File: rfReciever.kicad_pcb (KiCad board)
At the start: 2 copper layers, 5 x 8.2 mm, 37 parts, among them P2 USB_C_Plug_USB2.0, SW1 RF_RESET, SW2 RF_RESET, U1 CP2102N-Axx-xQFN20, X1 DigiXBeeRX900Micro

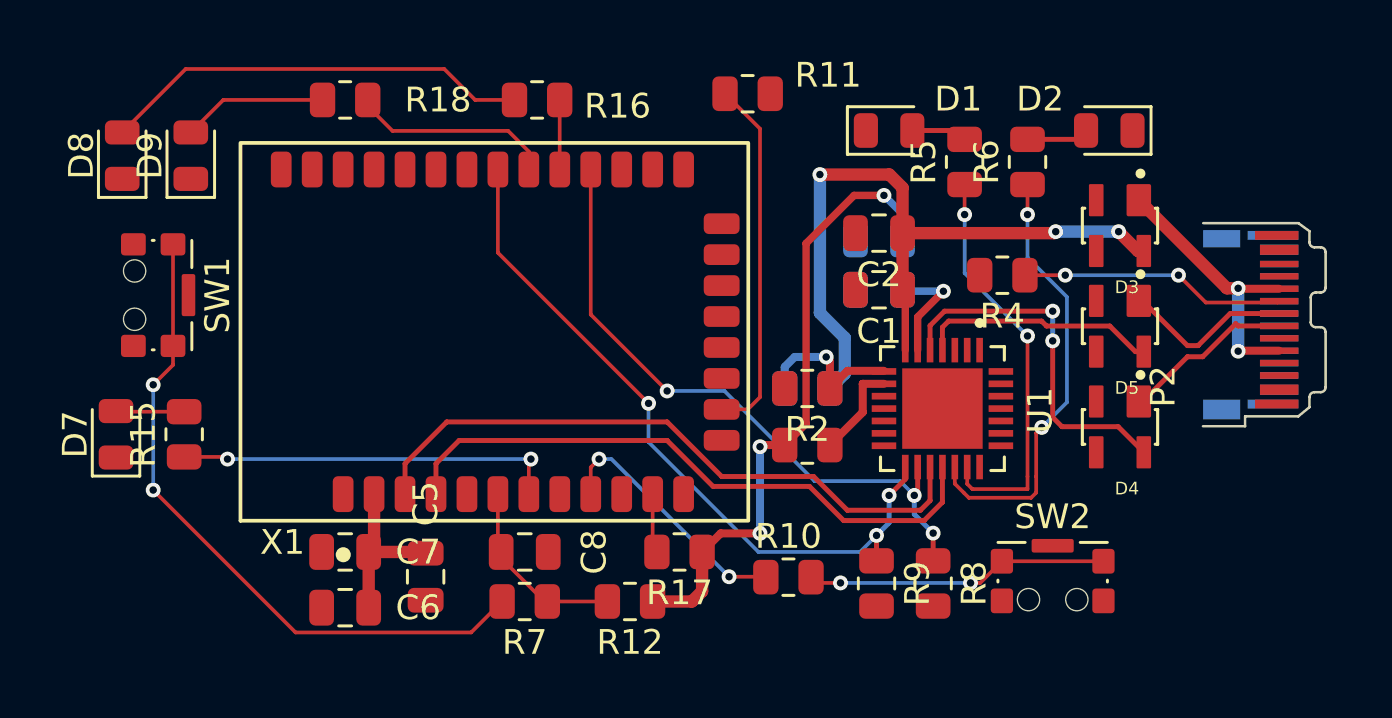
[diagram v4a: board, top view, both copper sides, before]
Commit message: V3 layout TODO: Rework to be 4 layer board
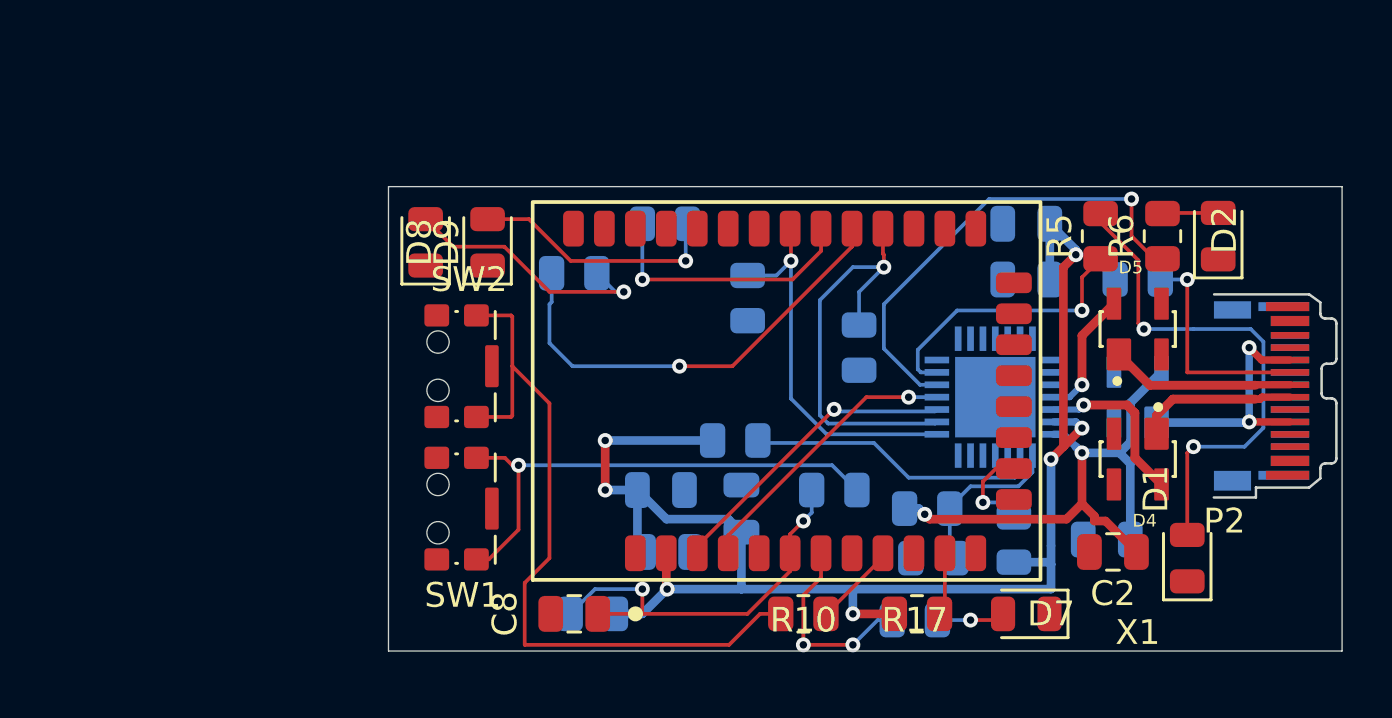
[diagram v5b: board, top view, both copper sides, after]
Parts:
- C1, C5, C6, C7, D3, R1, R11, R12, R15, R16, R18, R2, R4, R7, R8, R9, U1: moved to B.Cu
- moved D7 37.5 mm to (114.2, 82.0), turned to 180 degrees
- moved R15 30.4 mm to (109.8, 82.2), turned to 0 degrees
- moved SW2 25.6 mm to (91.2, 72.0), turned to -90 degrees
- moved D1 21.0 mm to (120.8, 79.8), turned to 90 degrees
- moved R11 21.0 mm to (113.8, 79.0), turned to 90 degrees
- moved C2 16.0 mm to (117.8, 79.5)
- moved SW1 15.0 mm to (91.2, 77.8)
- moved R18 13.8 mm to (99.7, 66.2), turned to 0 degrees
- moved C1 13.6 mm to (117.5, 79.0)
- moved R7 13.3 mm to (106.5, 77.0), turned to 0 degrees
- moved C6 13.2 mm to (99.8, 79.5), turned to 0 degrees
- moved C5 13.0 mm to (102.8, 77.8), turned to 90 degrees
- moved C7 13.0 mm to (99.5, 77.0), turned to 0 degrees
- moved D8 12.7 mm to (90.0, 67.0)
- moved R9 12.6 mm to (103.0, 69.2)
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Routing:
- net +3.3V: track 39.0 -> 61.3 mm, vias 4 -> 7
- net /BRIDGE_D1: track 2.26 -> 20.7 mm, vias 0 -> 2
- net Net-(R10-Pad2): track 12.3 -> 30.1 mm, vias 2 -> 0
- net /RF_DSLEEP: track 3.53 -> 18.2 mm, vias 0 -> 1
- net /RF_RXD: track 26.1 -> 12.3 mm, vias 0 -> 1
- net /RF_TXD: track 25.1 -> 11.5 mm, vias 0 -> 1
- net /UART_CTS: track 28.9 -> 15.4 mm, vias 3 -> 1
- net Net-(X1-SPI_N_SSEL/DIO17): track 14.6 -> 3.60 mm, vias 0 -> 1
- net /UART_RTS: track 26.1 -> 17.0 mm, vias 3 -> 1
- net /RF_RESET: track 8.09 -> 16.4 mm, vias 0 -> 2
- net /BRIDGE_3.3: track 3.97 -> 12.0 mm
- net /USB_OUT_D-: track 14.7 -> 6.82 mm, vias 2 -> 1
- net /RF_PWM: track 15.5 -> 7.99 mm
- net /RF_SLEEP: track 10.3 -> 3.41 mm, vias 2 -> 0
- net /RF_D8: track 17.4 -> 10.6 mm, vias 0 -> 1
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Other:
- board size 5 x 8.2 mm -> 38.5 x 18.8 mm

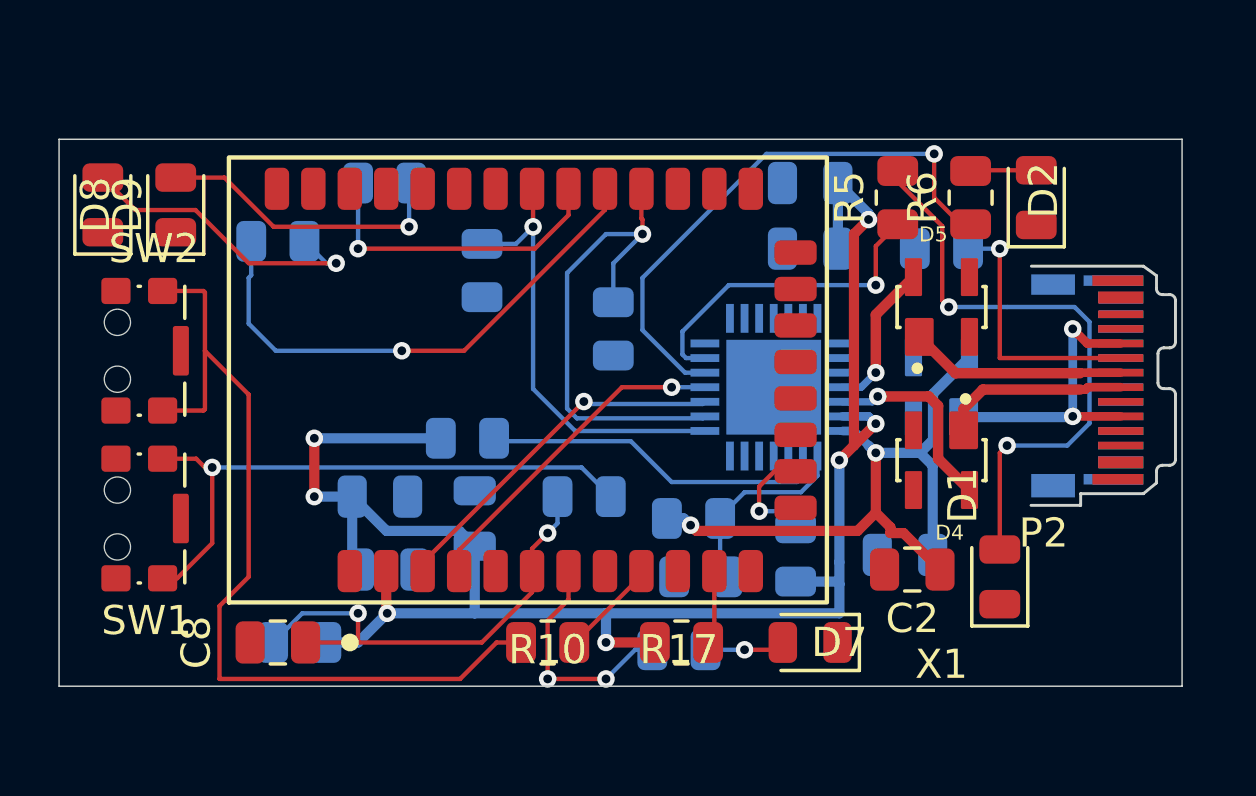
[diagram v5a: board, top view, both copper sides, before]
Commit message: 4 layer layout, new esd protection for USB
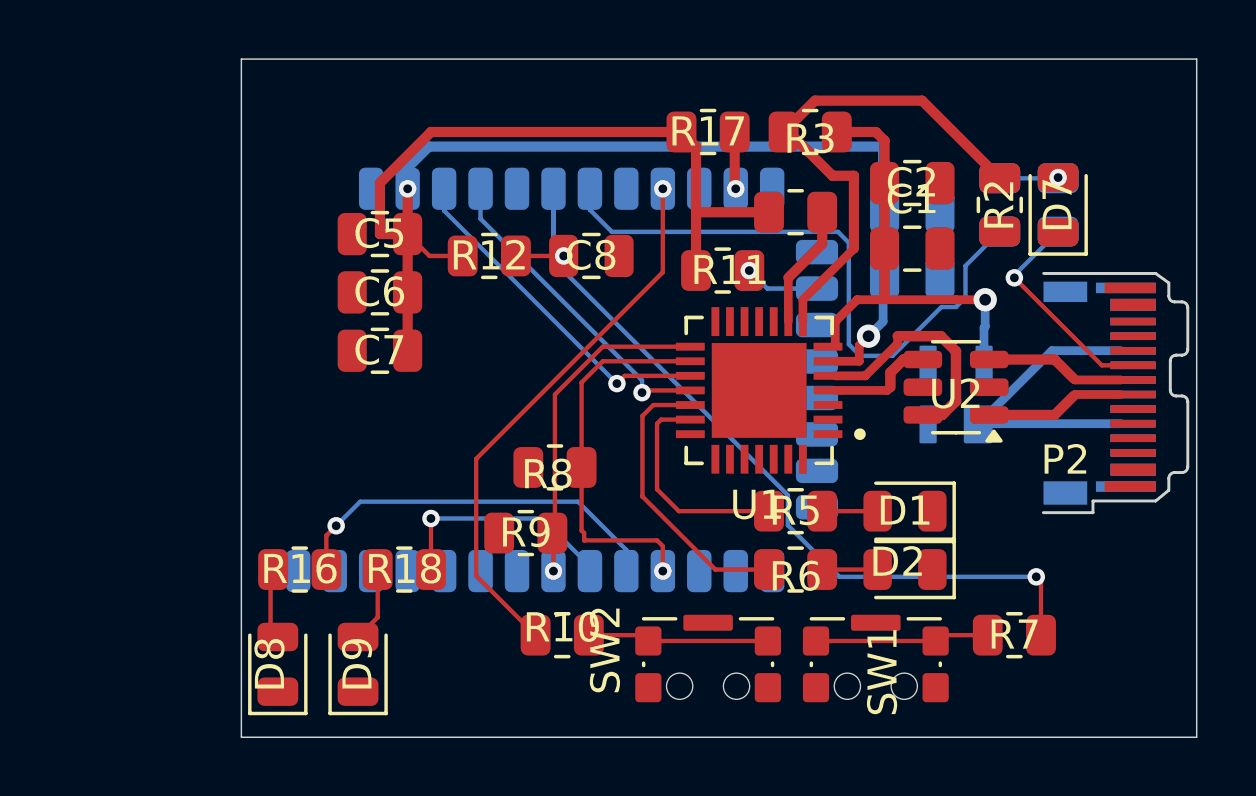
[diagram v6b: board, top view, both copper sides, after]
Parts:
- removed D4, D5: SP0503BAHTG, rfReciever-Footprints:SOT143
- added U2: USBLC6-2SC6, Package_TO_SOT_SMD:SOT-23-6, F.Cu at (119.2, 73.2)
- C1, C5, C6, C7, R1, R11, R12, R16, R18, R2, R3, R7, R8, R9, U1: moved to F.Cu
- X1: moved to B.Cu
- moved SW1 25.7 mm to (116.5, 82.8), turned to 0 degrees
- moved SW2 22.3 mm to (110.8, 82.8), turned to 0 degrees
- moved R15 18.8 mm to (120.8, 67.0), turned to 90 degrees
- moved R17 17.5 mm to (110.8, 64.5)
- moved D7 17.2 mm to (122.8, 67.0), turned to 90 degrees
- moved C8 17.1 mm to (106.8, 68.8), turned to 0 degrees
- moved D9 16.9 mm to (98.8, 82.8)
- moved D8 16.9 mm to (96.0, 82.8)
- moved R2 16.4 mm to (120.8, 67.0), turned to -90 degrees
- moved R7 15.5 mm to (121.2, 81.8), turned to 180 degrees
- moved R12 14.8 mm to (103.2, 68.8), turned to 0 degrees
- moved R6 14.1 mm to (113.8, 79.5), turned to 0 degrees
- moved R3 13.8 mm to (114.2, 64.5), turned to 180 degrees
- moved R1 13.7 mm to (113.8, 67.2)
- moved D2 13.5 mm to (117.5, 79.5), turned to 180 degrees
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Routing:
- net Net-(R10-Pad2): track 30.1 -> 6.22 mm
- net /BRIDGE_D1: track 20.7 -> 1.90 mm, vias 2 -> 0
- net /RF_SLEEP: track 3.41 -> 18.9 mm, vias 0 -> 1
- net /RF_SW_RSTO: track 20.7 -> 5.97 mm, vias 1 -> 0
- net /RF_RESET: track 16.4 -> 30.3 mm
- net /RF_PWM: track 7.99 -> 21.3 mm, vias 2 -> 0
- net /BRIDGE_VBUS: track 6.76 -> 17.7 mm
- net Net-(U1-~{RXT}/GPIO.3): track 19.4 -> 9.93 mm, vias 1 -> 0
- net /RF_D8: track 10.6 -> 2.35 mm, vias 1 -> 0
- net /BRIDGE_3.3: track 12.0 -> 4.23 mm
- net +5V: track 23.1 -> 15.5 mm, vias 2 -> 1
- net /RF_D9: track 10.2 -> 2.59 mm, vias 1 -> 0
- net +3.3V: track 61.3 -> 55.4 mm, vias 7 -> 2
- net /RF_DSLEEP: track 18.2 -> 13.3 mm
- net /UART_CTS: track 15.4 -> 11.5 mm
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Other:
- board size 38.5 x 18.8 mm -> 32.8 x 23.2 mm
- copper layers 2 -> 4

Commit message: Fixed up layout + shematic
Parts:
- added C9: 1u, Capacitor_SMD:C_0805_2012Metric, F.Cu at (106.8, 65.8)
- added R13: 1k, Resistor_SMD:R_0805_2012Metric, F.Cu at (107.8, 63.0)
- C5, C6, C7: moved to B.Cu
- R15, R4: moved to F.Cu
- SW2: value RF_RESET -> RF_SLEEP
- moved R7 28.8 mm to (97.0, 66.2)
- moved SW1 26.9 mm to (98.0, 63.2), turned to 180 degrees
- moved SW2 19.5 mm to (111.8, 63.2), turned to 180 degrees
- moved R10 13.4 mm to (107.8, 68.5), turned to -90 degrees
- moved D8 12.0 mm to (97.0, 70.8), turned to 0 degrees
- moved C7 10.8 mm to (103.0, 61.8), turned to 0 degrees
- moved D9 10.1 mm to (97.0, 72.8), turned to 0 degrees
- moved C8 9.76 mm to (97.0, 68.2), turned to 180 degrees
- moved R16 9.52 mm to (100.5, 70.8)
- moved R17 7.52 mm to (117.8, 61.8)
- moved R18 6.75 mm to (100.5, 72.8)
- moved C6 6.73 mm to (103.0, 64.2), turned to 0 degrees
- moved D7 4.59 mm to (125.0, 63.0), turned to 180 degrees
- moved R15 4.07 mm to (121.5, 63.0), turned to 0 degrees
- moved R2 4.07 mm to (117.8, 64.2), turned to 0 degrees
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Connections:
- net /RF_SW_RSTO renamed /RF_SW_RESET
- D3 pad 1: Net-(D3-Pad1) -> +5V
- P2 pad A4: Net-(D3-Pad1) -> +5V
- P2 pad A9: Net-(D3-Pad1) -> +5V
- P2 pad B4: Net-(D3-Pad1) -> +5V
- P2 pad B9: Net-(D3-Pad1) -> +5V
- R10 pad 2: Net-(R10-Pad2) -> +3.3V
- SW2 pad 1: Net-(R10-Pad2) -> /RF_SW_SLEEP
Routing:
- net /RF_RESET: track 30.3 -> 12.6 mm, vias 2 -> 1
- net /RF_SLEEP: track 18.9 -> 6.50 mm
- net Net-(D3-Pad1): track 10.8 -> 0.00 mm
- net /BRIDGE_VBUS: track 17.7 -> 8.27 mm
- net +5V: track 15.5 -> 24.4 mm
- net +3.3V: track 55.4 -> 48.4 mm
- net /RF_SW_SLEEP: track 0.00 -> 6.87 mm
- net Net-(R10-Pad2): track 6.22 -> 0.00 mm
- net /USB_OUT_D-: track 8.10 -> 2.36 mm
- net /RF_PWM: track 21.3 -> 18.7 mm, vias 0 -> 1
- net /USB_OUT_D+: track 3.73 -> 5.95 mm
- net /RF_ASSOCIATE: track 8.04 -> 10.2 mm
- net /USB_IN_D+: track 4.80 -> 6.76 mm
- net /RF_BOOTMODE: track 1.96 -> 0.00 mm, vias 1 -> 0
- net /BRIDGE_3.3: track 4.23 -> 2.29 mm
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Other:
- board size 32.8 x 23.2 mm -> 32.8 x 20.5 mm

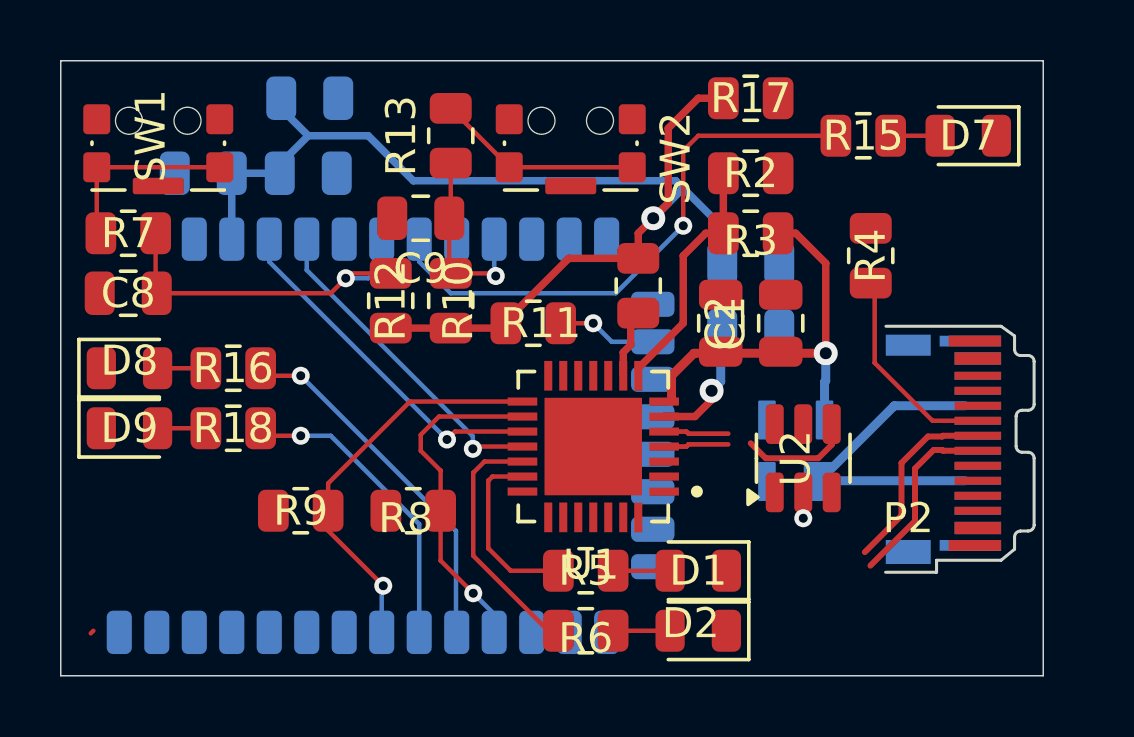
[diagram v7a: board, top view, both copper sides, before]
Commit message: new molex connector, final layout
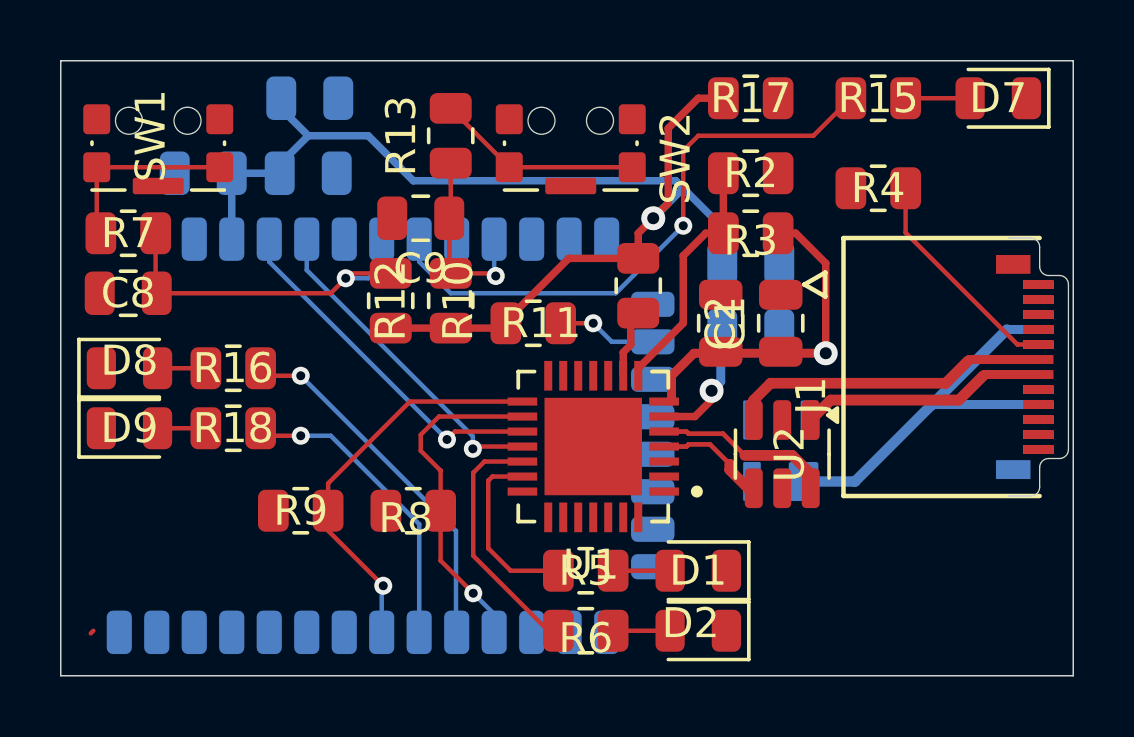
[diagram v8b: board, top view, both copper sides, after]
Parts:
- removed P2: USB_C_Plug_USB2.0, Connector_USB:USB_C_Plug_JAE_DX07P024AJ1
- added J1: 1054440001, rfReciever-Footprints:MOLEX_1054440001, F.Cu at (128.3, 70.7)
- moved R4 2.26 mm to (122.0, 64.8), turned to 180 degrees
- moved D7 1.60 mm to (126.0, 61.8)
- moved R15 1.35 mm to (122.0, 61.8)
- moved U2 0.71 mm to (118.8, 73.6), turned to -90 degrees
- moved D3 0.50 mm to (118.8, 73.5)
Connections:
- D3 pad 1: +5V -> /MLX(VBUS)
- U2 pad 1: /USB_IN_D- -> /MLX(D-)
- U2 pad 3: /USB_IN_D+ -> /MLX(D+)
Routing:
- net /MLX(VBUS): track 0.00 -> 13.5 mm
- net +5V: track 24.4 -> 11.3 mm
- net /MLX(D+): track 0.00 -> 10.7 mm
- net /MLX(D-): track 0.00 -> 8.22 mm
- net /USB_IN_D+: track 6.76 -> 0.00 mm
- net /USB_IN_D-: track 6.58 -> 0.00 mm
- net /USB_OUT_D-: track 2.36 -> 6.07 mm
- net /USB_OUT_D+: track 5.95 -> 3.79 mm
- net /RF_PWM: track 18.7 -> 19.7 mm
- net GND: track 0.86 -> 0.00 mm, vias 1 -> 0
- net /RF_D7: track 1.65 -> 2.15 mm
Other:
- board size 32.8 x 20.5 mm -> 33.8 x 20.5 mm
